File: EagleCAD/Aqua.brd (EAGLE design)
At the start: 25.1 x 47 mm, 13 parts, among them IC1 TINY13-20PU, Q1 IRF3704

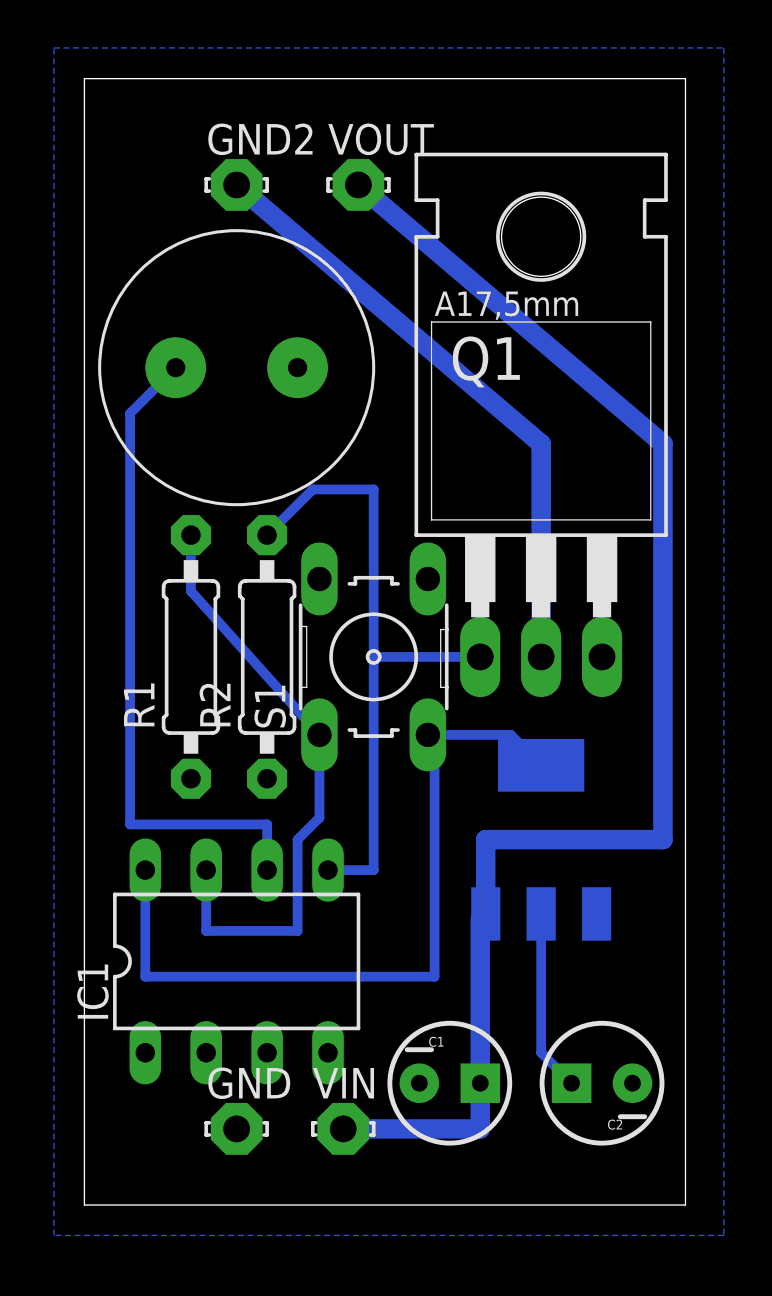
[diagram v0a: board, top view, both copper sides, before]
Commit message: Time count improvement
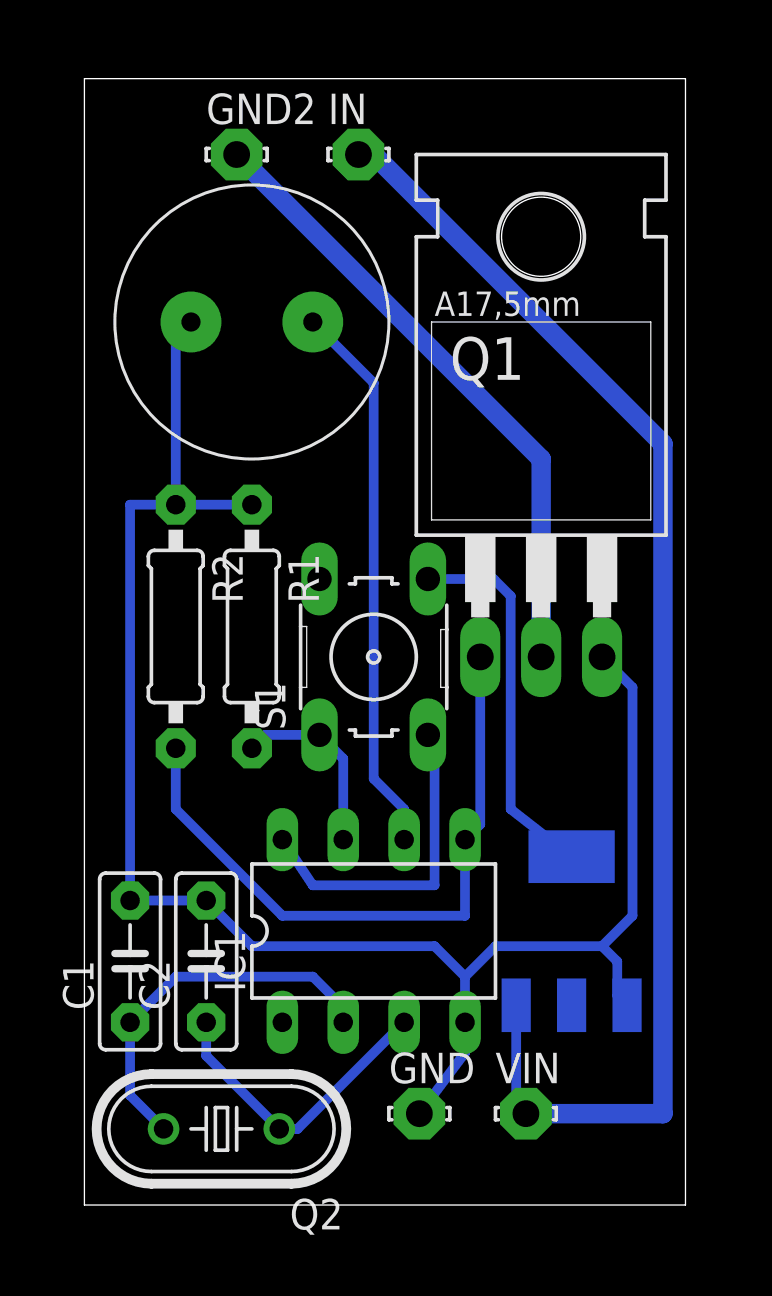
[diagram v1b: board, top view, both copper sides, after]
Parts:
- removed VOUT: LSP11, solpad:LSP11
- added IN: LSP11, solpad:LSP11
- added Q2: 20MHz, adafruit:HC49U-V
- C1: value 100uF -> 22pF; device SparkFun-Capacitors:CPOL-RADIAL-10UF-25V -> capacitor-wima:C5B2.5
- C2: value 10uF -> 22pF; device SparkFun-Capacitors:CPOL-RADIAL-10UF-25V -> capacitor-wima:C5B2.5
- moved C2 17.3 mm to (5.08, 10.2), turned to 90 degrees
- moved C1 14.3 mm to (1.91, 10.2), turned to 90 degrees
- moved GND 7.65 mm to (14.0, 3.81)
- moved VIN 7.65 mm to (18.4, 3.81)
- moved IC1 5.85 mm to (12.1, 11.4)
- moved R2 4.02 mm to (3.81, 24.1), turned to 270 degrees
- moved U1 4.02 mm to (20.3, 11.4)
- moved R1 2.84 mm to (6.99, 24.1), turned to 270 degrees
- moved U$1 2.01 mm to (6.99, 36.8), turned to 0 degrees
- moved GND2 1.27 mm to (6.35, 43.8)
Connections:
- removed net OUT: C2.1, U1.2
- removed net VIN: C1.1, U1.3, VIN.MP, VOUT.MP
- new net N$3: C1.1, IC1.2, Q2.2
- new net N$6: C2.1, IC1.3, Q2.1
- new net N$7: IC1.8, S1.3
- new net N$8: IN.MP, U1.3, VIN.MP
- net +5V: now also S1.4; no longer IC1.8, S1.3
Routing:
- net GND: track 0.00 -> 73.4 mm
- net VIN: track 58.4 -> 0.00 mm
- net N$8: track 0.00 -> 56.0 mm
- net N$4: track 25.3 -> 7.83 mm
- net +5V: track 32.1 -> 15.9 mm
- net N$3: track 0.00 -> 15.9 mm
- net N$7: track 0.00 -> 13.8 mm
- net N$6: track 0.00 -> 12.8 mm
- net OUT: track 7.59 -> 0.00 mm
- net N$2: track 27.5 -> 23.2 mm
- net N$1: track 25.6 -> 26.2 mm
- removed copper zone on layer 16, net GND
